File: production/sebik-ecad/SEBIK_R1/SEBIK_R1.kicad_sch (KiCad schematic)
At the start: 87 parts, among them J1 Conn_01x06_Male, J10 Conn_01x02_Male, J11 Conn_01x03_Male, J12 Conn_01x02_Male, J13 Conn_01x02_Male, J2 Conn_01x02_Male, J3 Conn_01x02_Male, J4 Conn_01x02_Male, J5 Conn_01x02_Male, J6 Conn_01x02_Male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

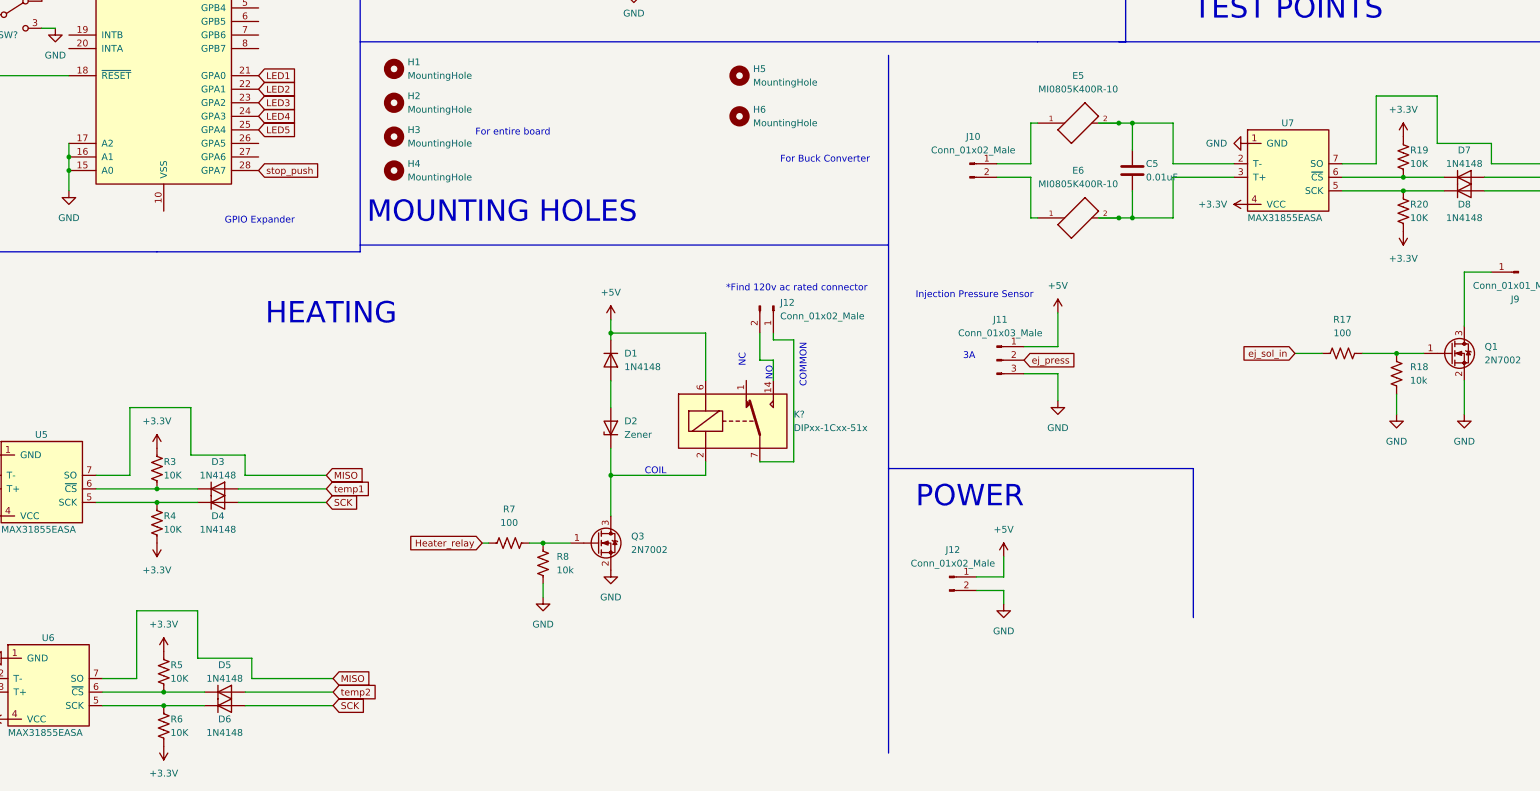
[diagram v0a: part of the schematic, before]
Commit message: took off pulldown resistors on thermocouple sensors
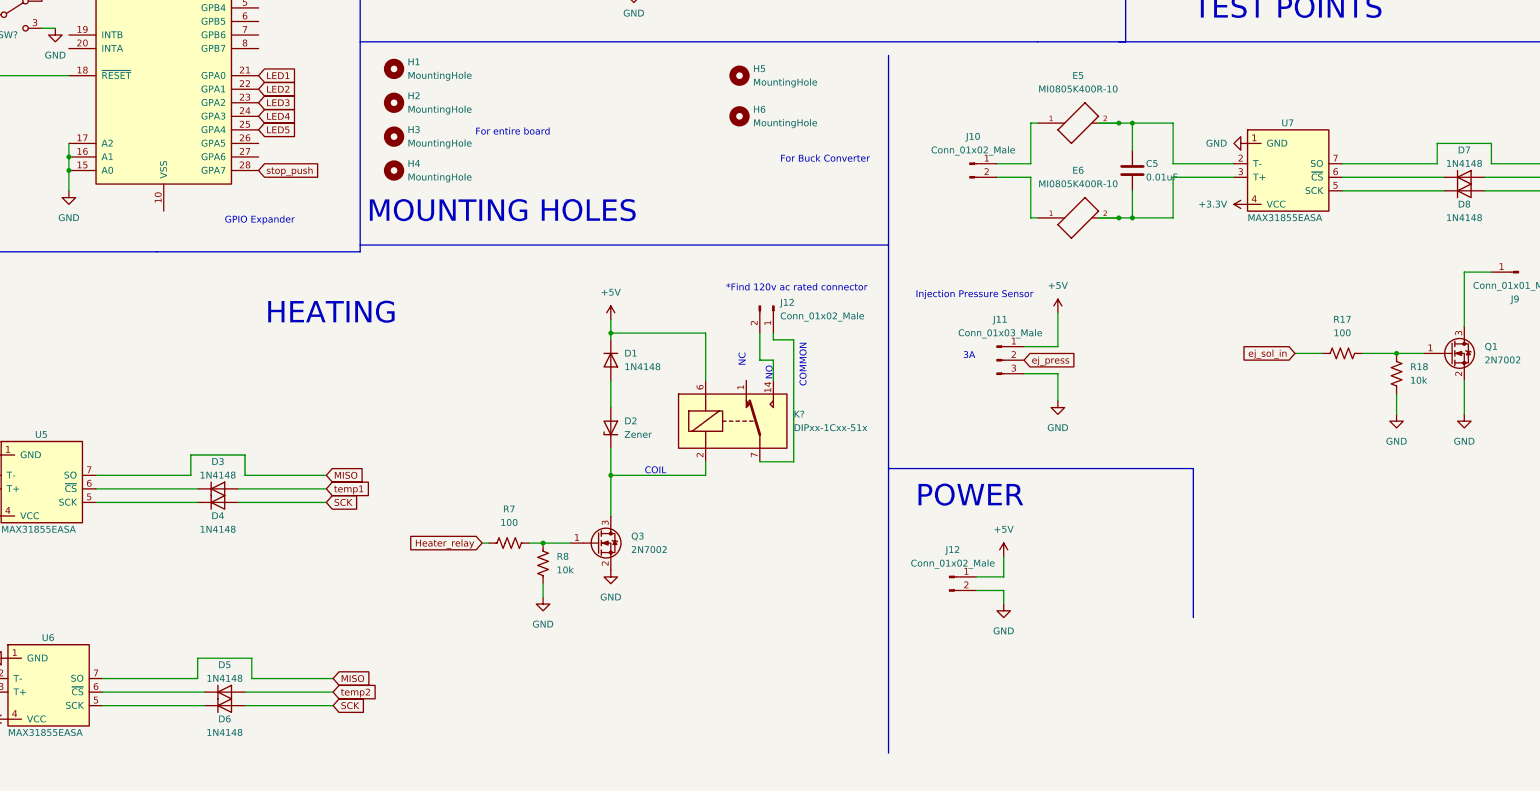
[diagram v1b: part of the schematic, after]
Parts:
- removed R19, R20, R3, R4, R5, R6: 10K, Resistor_SMD:R_0805_2012Metric, symbol Device:R_US
